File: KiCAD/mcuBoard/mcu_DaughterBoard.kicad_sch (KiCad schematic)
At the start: 23 parts, among them SW1 NRST, SW2 BOOT0, U1 AP2112K-3.3, U2 STM32F072CBTx, U3 USBLC6-2SC6

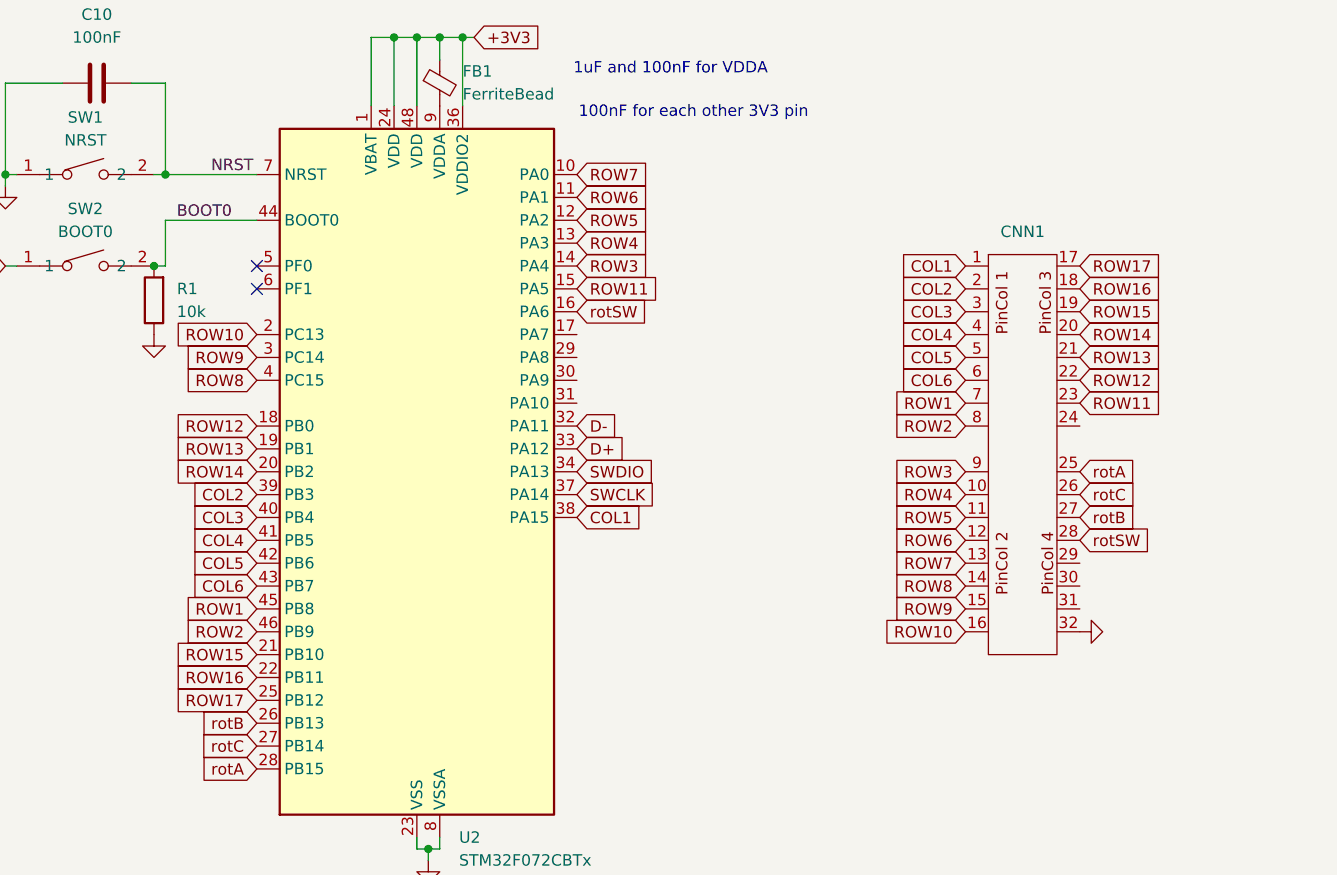
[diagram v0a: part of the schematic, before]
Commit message: Fixed net names, columns and rows were switched.
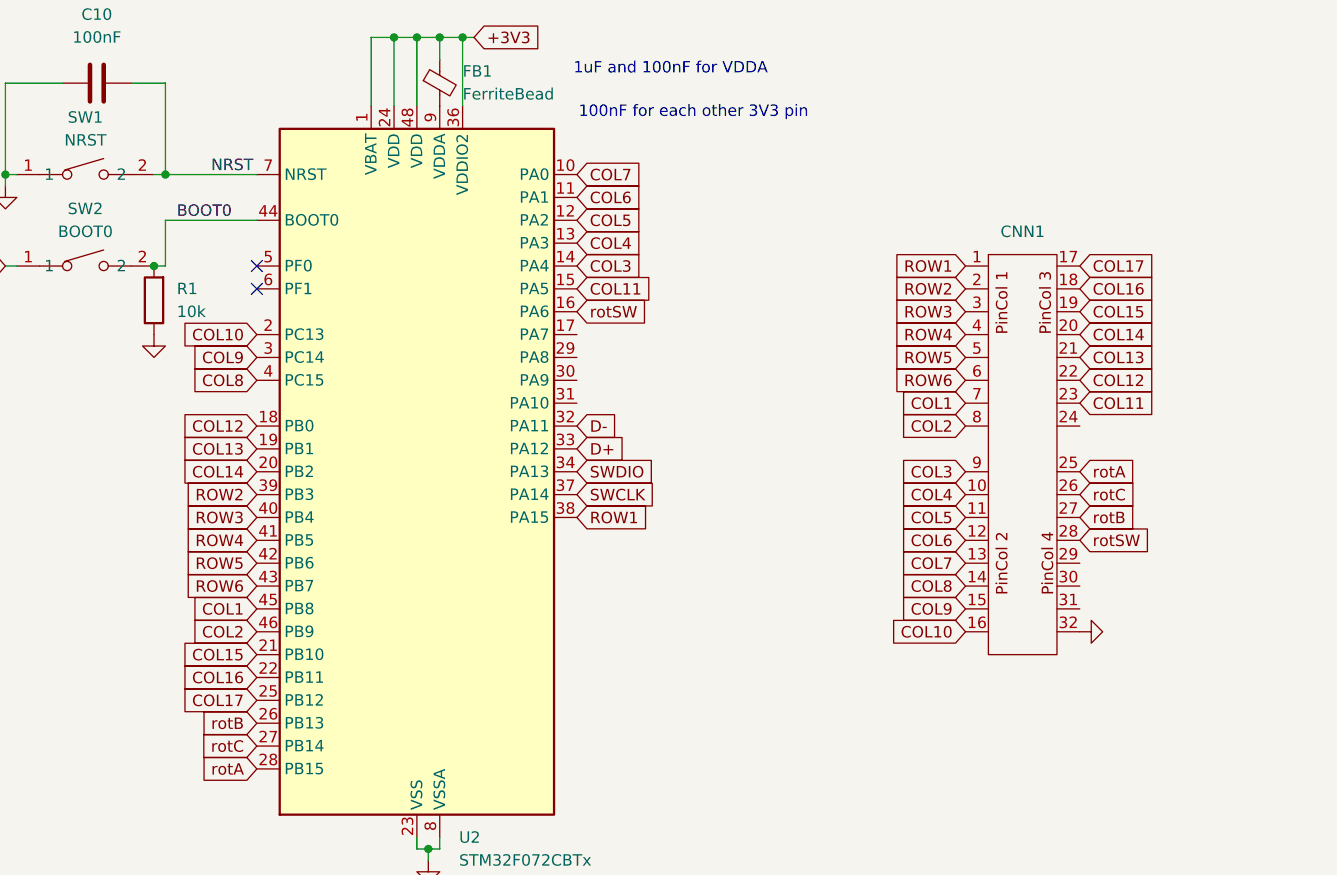
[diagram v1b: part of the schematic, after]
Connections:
- net COL1: now also CNN1.7, U2.45 (PB8); no longer CNN1.1, U2.38 (PA15)
- net COL2: now also CNN1.8, U2.46 (PB9); no longer CNN1.2, U2.39 (PB3)
- net COL3: now also CNN1.9, U2.14 (PA4); no longer CNN1.3, U2.40 (PB4)
- net COL4: now also CNN1.10, U2.13 (PA3); no longer CNN1.4, U2.41 (PB5)
- net COL5: now also CNN1.11, U2.12 (PA2); no longer CNN1.5, U2.42 (PB6)
- net COL6: now also CNN1.12, U2.11 (PA1); no longer CNN1.6, U2.43 (PB7)
- net ROW1: now also CNN1.1, U2.38 (PA15); no longer CNN1.7, U2.45 (PB8)
- net ROW2: now also CNN1.2, U2.39 (PB3); no longer CNN1.8, U2.46 (PB9)
- net ROW3: now also CNN1.3, U2.40 (PB4); no longer CNN1.9, U2.14 (PA4)
- net ROW4: now also CNN1.4, U2.41 (PB5); no longer CNN1.10, U2.13 (PA3)
- net ROW5: now also CNN1.5, U2.42 (PB6); no longer CNN1.11, U2.12 (PA2)
- net ROW6: now also CNN1.6, U2.43 (PB7); no longer CNN1.12, U2.11 (PA1)
- net ROW10 renamed COL10
- net ROW11 renamed COL11
- net ROW12 renamed COL12
- net ROW13 renamed COL13
- net ROW14 renamed COL14
- net ROW15 renamed COL15
- net ROW16 renamed COL16
- net ROW17 renamed COL17
- net ROW7 renamed COL7
- net ROW8 renamed COL8
- net ROW9 renamed COL9

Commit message: Added SWD connector headers. Touched up routing on both boards.
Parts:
- added J1: Conn_SWD, Connector_PinHeader_2.54mm:PinHeader_1x04_P2.54mm_Vertical, symbol Connector_Generic:Conn_01x04
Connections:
- net +3V3: now also J1.4 (Pin_4)
- net GND: now also J1.1 (Pin_1)
- net SWCLK: now also J1.2 (Pin_2)
- net SWDIO: now also J1.3 (Pin_3)
- no-connect marks 4 -> 9
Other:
- note added: "Connector"
- note added: "Linear Voltage Regulator"
- note added: "STM32F0 MicroController"
- note added: "SWD Headers"
- note added: "USB 2.0 Type C"
- moved on the sheet: C10, FB1, R1, SW1, SW2, U2
